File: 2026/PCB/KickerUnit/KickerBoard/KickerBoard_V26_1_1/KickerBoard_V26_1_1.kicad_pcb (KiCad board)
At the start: 2 copper layers, 98 x 90 mm, 73 parts, among them J1 MOLEX MINISPOX, J2 Conn_01x07_Socket, Q1 Q_NMOS_GDS, Q2 FDS2582, SW1 SW_Push, SW2 SW_Push, T1 750032052, U1 STM32F303K8Tx, U2 MCP1703AT, U3 LMR51450SDRRR, U4 LT3751UFD

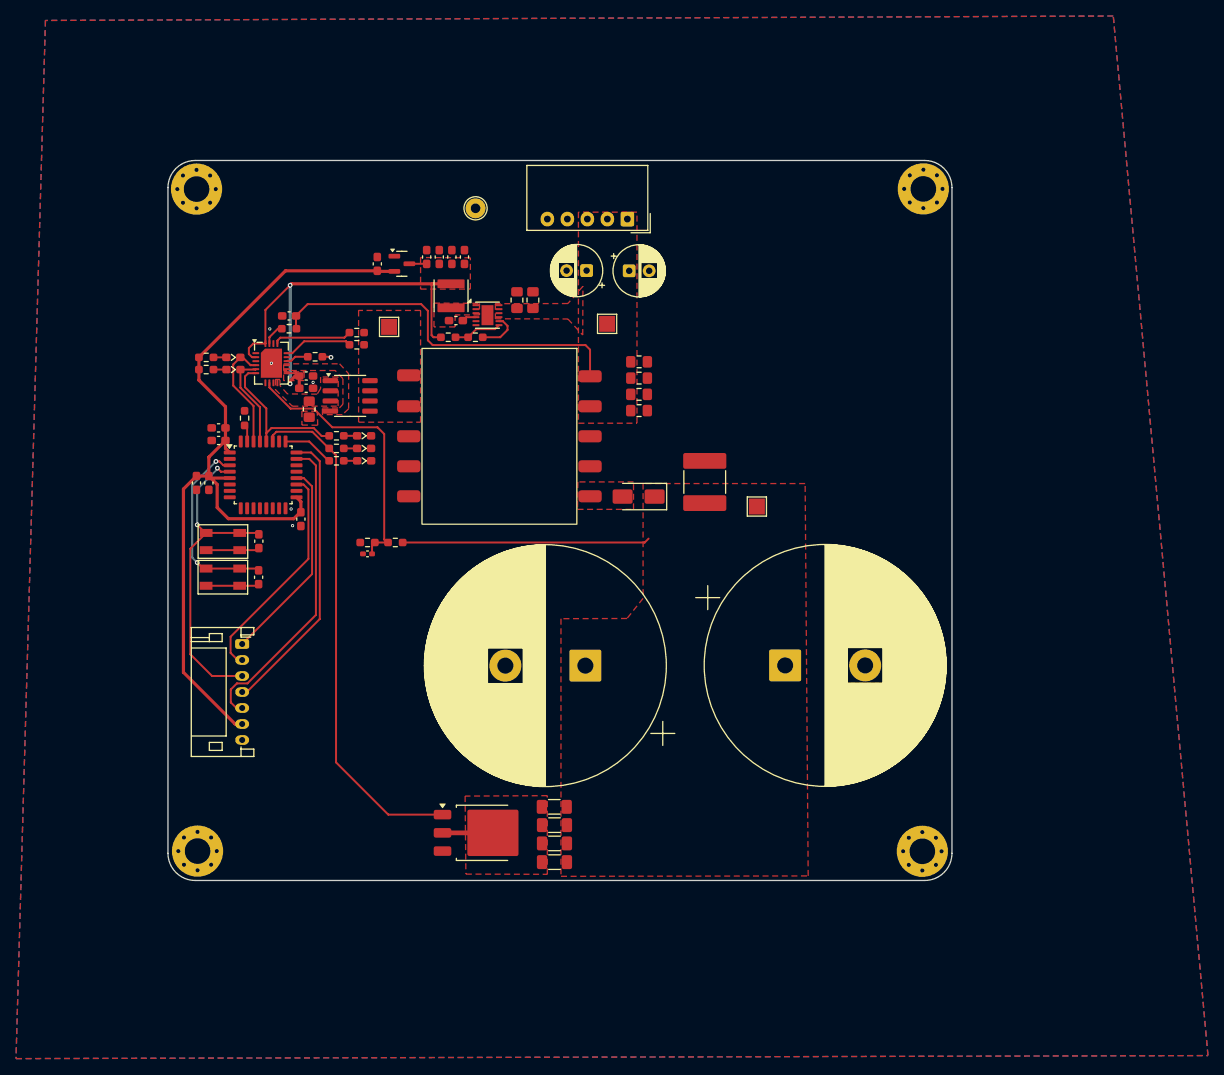
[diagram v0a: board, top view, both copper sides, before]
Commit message: アートワーク完成、製造ファイル出力
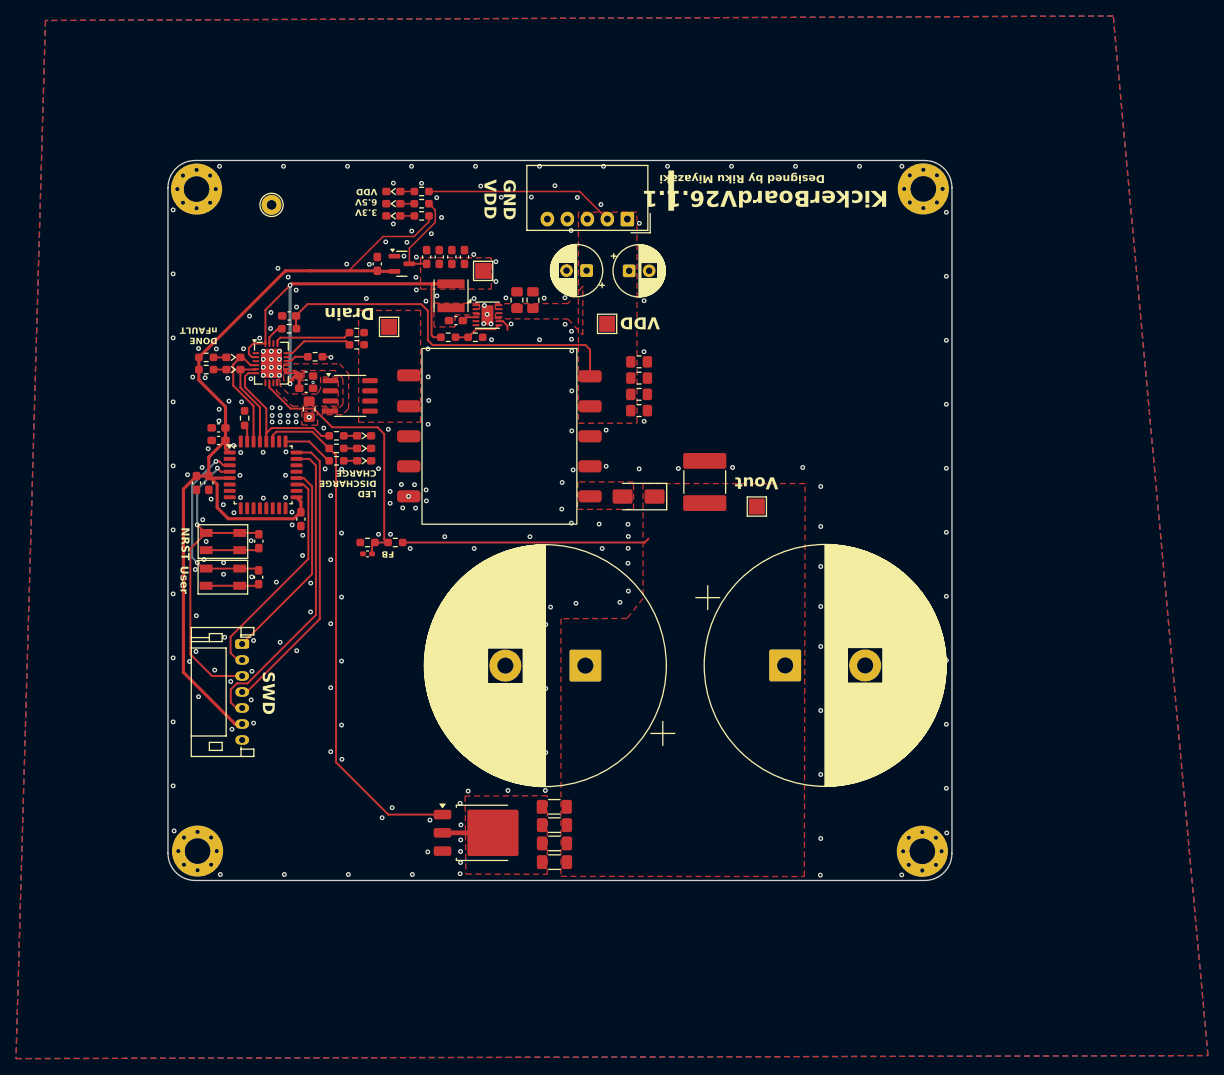
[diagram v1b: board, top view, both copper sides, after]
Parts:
- added D7: LED, KickerUnit_LIB_FTP:LED, F.Cu at (7.90, -12.2)
- added D8: LED, KickerUnit_LIB_FTP:LED, F.Cu at (7.90, -10.7)
- added D9: LED, KickerUnit_LIB_FTP:LED, F.Cu at (7.90, -9.15)
- added R20: 1k, Resistor_SMD:R_0603_1608Metric_Pad0.98x0.95mm_HandSolder, F.Cu at (11.4, -12.2)
- added R21: 1k, Resistor_SMD:R_0603_1608Metric_Pad0.98x0.95mm_HandSolder, F.Cu at (11.4, -10.7)
- added R22: 1k, Resistor_SMD:R_0603_1608Metric_Pad0.98x0.95mm_HandSolder, F.Cu at (11.4, -9.15)
- added TP5: 6V, TestPoint:TestPoint_Pad_2.0x2.0mm, F.Cu at (19.1, -2.27)
- L1: value 4.7uF -> 4.7u
- moved TP4 25.5 mm to (-7.33, -10.5)
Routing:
- net VDD: track 46.8 -> 70.6 mm
- net +3.3V: track 105.0 -> 123.1 mm
- net +6V: track 60.1 -> 69.2 mm
- net GND: track 19.8 -> 16.3 mm, vias 6 -> 259
- net Net-(D9-A): track 0.00 -> 1.75 mm
- net Net-(D8-A): track 0.00 -> 1.75 mm
- net Net-(D7-A): track 0.00 -> 1.75 mm
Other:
- board text added: "3.3V 6.5V VDD"
- board text added: "DONE nFAULT"
- board text added: "Designed by Riku Miyazaki"
- board text added: "Drain"
- board text added: "FB"
- board text added: "GND VDD"
- board text added: "KickerBoardV26.1.1"
- board text added: "LED DISCHARGE CHARGE"
- board text added: "NRST"
- board text added: "SWD"
- board text added: "User"
- board text added: "VDD"
- board text added: "Vout"
